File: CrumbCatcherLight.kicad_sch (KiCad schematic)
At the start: 10 parts, among them J1 USB_C_Receptacle, U0 PCB, U1 ECMF02-2AMX6

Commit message: Clear ERC's
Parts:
- renumbered U0 to U2
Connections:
- no-connect marks 16 -> 17
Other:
- sheet RP2040: file mad_lib/schematics/MCU/MCU_RP2040.kicad_sch -> mad_lib/schematics/Keyboard Controllers/Controller_RP2040.kicad_sch
- sheet RP2040 ports: added LED_DO; removed none
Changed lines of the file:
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@@
 	)
 	(no_connect
+		(at 177.165 104.14)
+	)
+	(no_connect
 		(at 175.26 69.85)
 	)
@@
 	(wire
 		(pts
+			(xy 172.72 104.14) (xy 177.165 104.14)
+		)
+		(stroke
+			(width 0)
+			(type default)
+		)
+	)
+	(wire
+		(pts
 			(xy 47.625 57.785) (xy 48.895 57.785)
 		)
@@
 		(dnp no)
 		(fields_autoplaced yes)
-		(property "Reference" "#PWR07"
+		(property "Reference" "#PWR05"
 			(at 149.86 62.23 0)
 			(effects
@@
 			(project "CrumbCatcherLight"
 				(path "/eedae293-eb5b-47bd-b383-bccfdf81bf72"
-					(reference "#PWR07")
+					(reference "#PWR05")
 					(unit 1)
 				)
@@
 		(on_board yes)
 		(dnp no)
-		(property "Reference" "U0"
+		(property "Reference" "U2"
 			(at 171.45 190.4999 0)
 			(effects
@@
 			(project "CrumbCatcherLight"
 				(path "/eedae293-eb5b-47bd-b383-bccfdf81bf72"
-					(reference "U0")
+					(reference "U2")
 					(unit 1)
 				)
@@
 		(dnp no)
 		(fields_autoplaced yes)
-		(property "Reference" "#PWR08"
+		(property "Reference" "#PWR07"
 			(at 184.785 61.595 0)
 			(effects
@@
 			(project "CrumbCatcherLight"
 				(path "/eedae293-eb5b-47bd-b383-bccfdf81bf72"
-					(reference "#PWR08")
+					(reference "#PWR07")
 					(unit 1)
 				)
@@
 		(on_board yes)
 		(dnp no)
-		(property "Reference" "#PWR09"
+		(property "Reference" "#PWR06"
 			(at 150.495 114.935 0)
 			(effects
@@
 			(project "CrumbCatcherLight"
 				(path "/eedae293-eb5b-47bd-b383-bccfdf81bf72"
-					(reference "#PWR09")
+					(reference "#PWR06")
 					(unit 1)
 				)
@@
 		(on_board yes)
 		(dnp no)
-		(property "Reference" "#PWR05"
+		(property "Reference" "#PWR08"
 			(at 185.42 114.935 0)
 			(effects
@@
 			(project "CrumbCatcherLight"
 				(path "/eedae293-eb5b-47bd-b383-bccfdf81bf72"
-					(reference "#PWR05")
+					(reference "#PWR08")
 					(unit 1)
 				)
@@
 			)
 		)
-		(property "Sheetfile" "mad_lib/schematics/MCU/MCU_RP2040.kicad_sch"
+		(property "Sheetfile" "mad_lib/schematics/Keyboard Controllers/Controller_RP2040.kicad_sch"
 			(at 153.67 107.8996 0)
 			(effects
@@
 			)
 		)
+		(pin "LED_DO" output
+			(at 172.72 104.14 0)
+			(effects
+				(font
+					(size 1.27 1.27)
+				)
+				(justify right)
+			)
+		)
 		(instances
 			(project "CrumbCatcherLight"
 				(path "/eedae293-eb5b-47bd-b383-bccfdf81bf72"
-					(page "2")
+					(page "4")
 				)
 			)

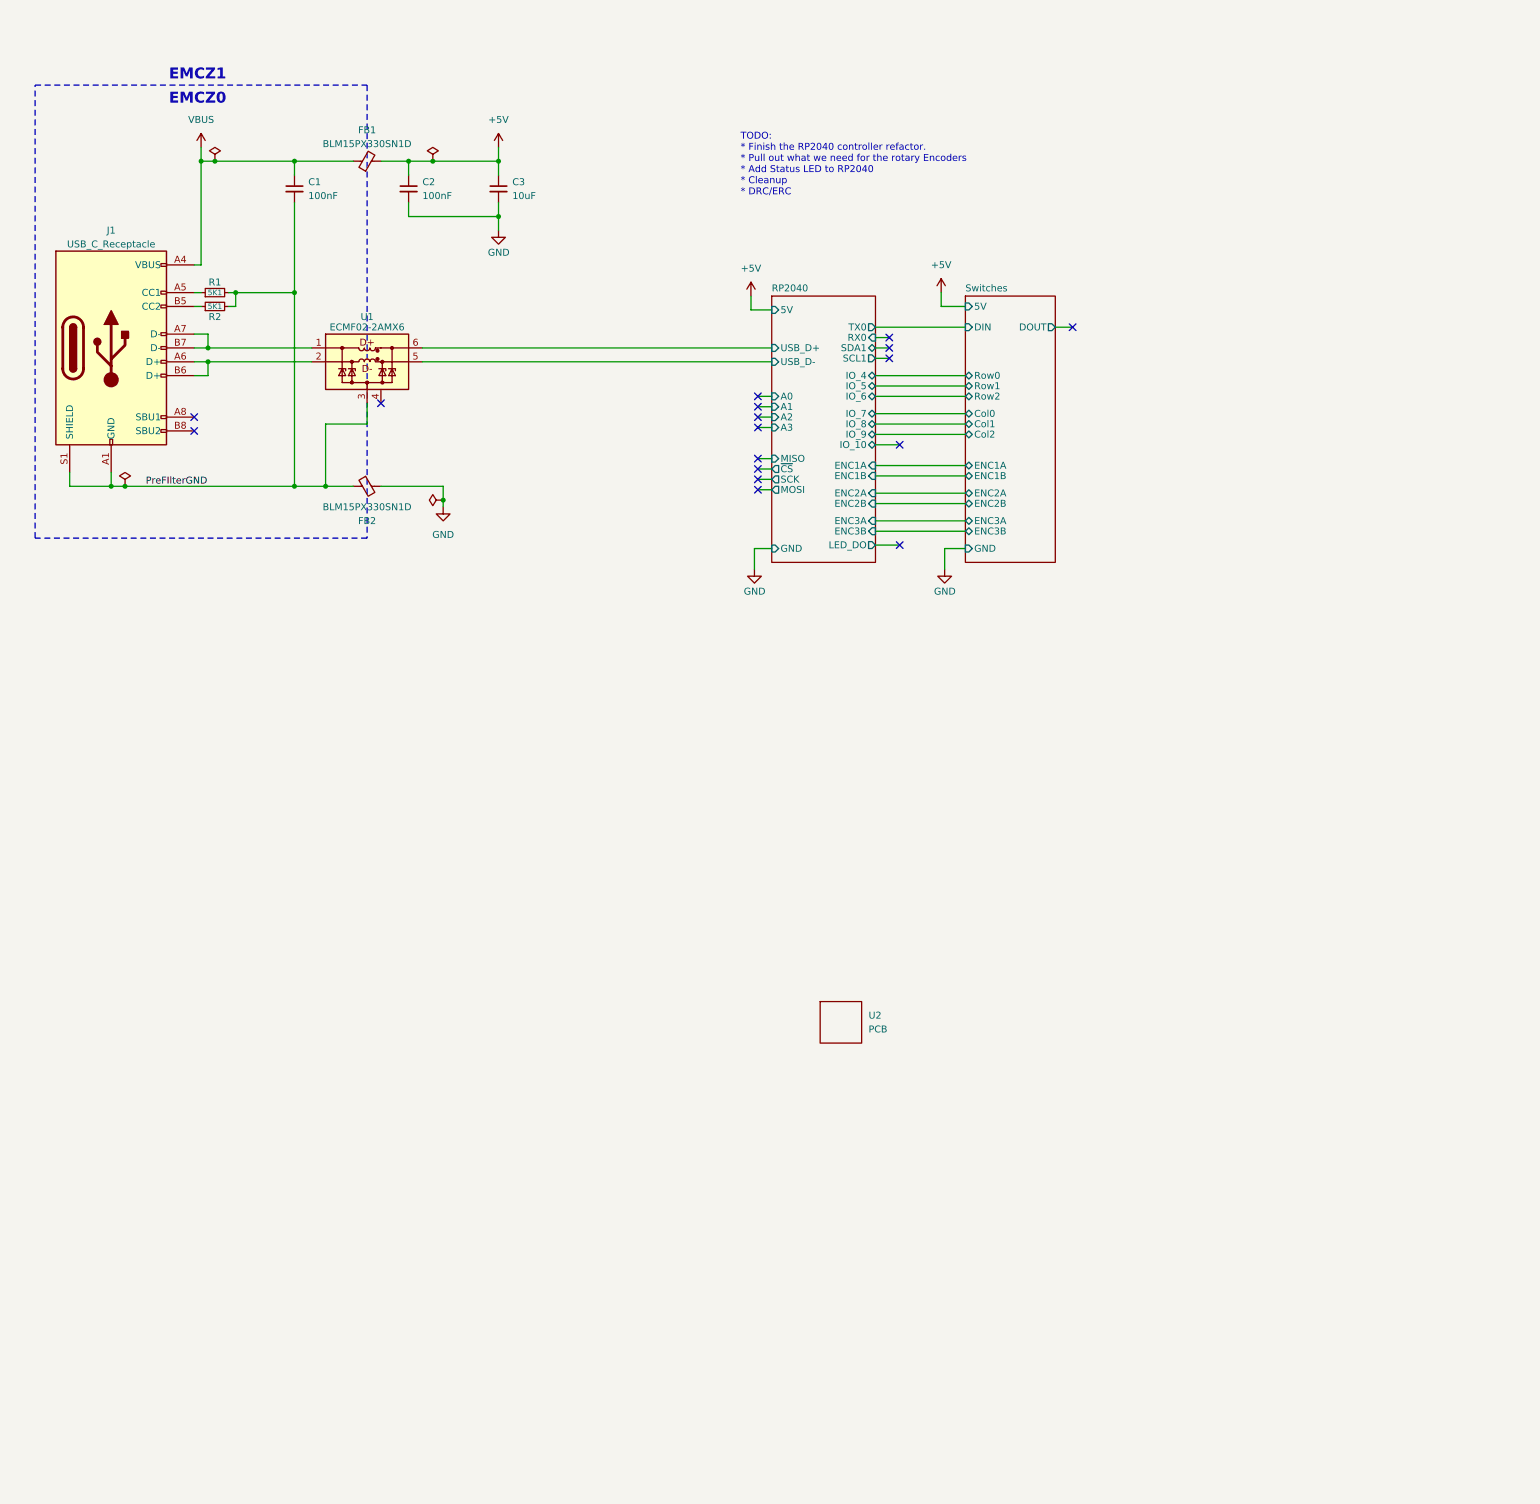
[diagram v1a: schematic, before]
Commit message: Add some reference circuits, add bq240xx, start to addnRF52840
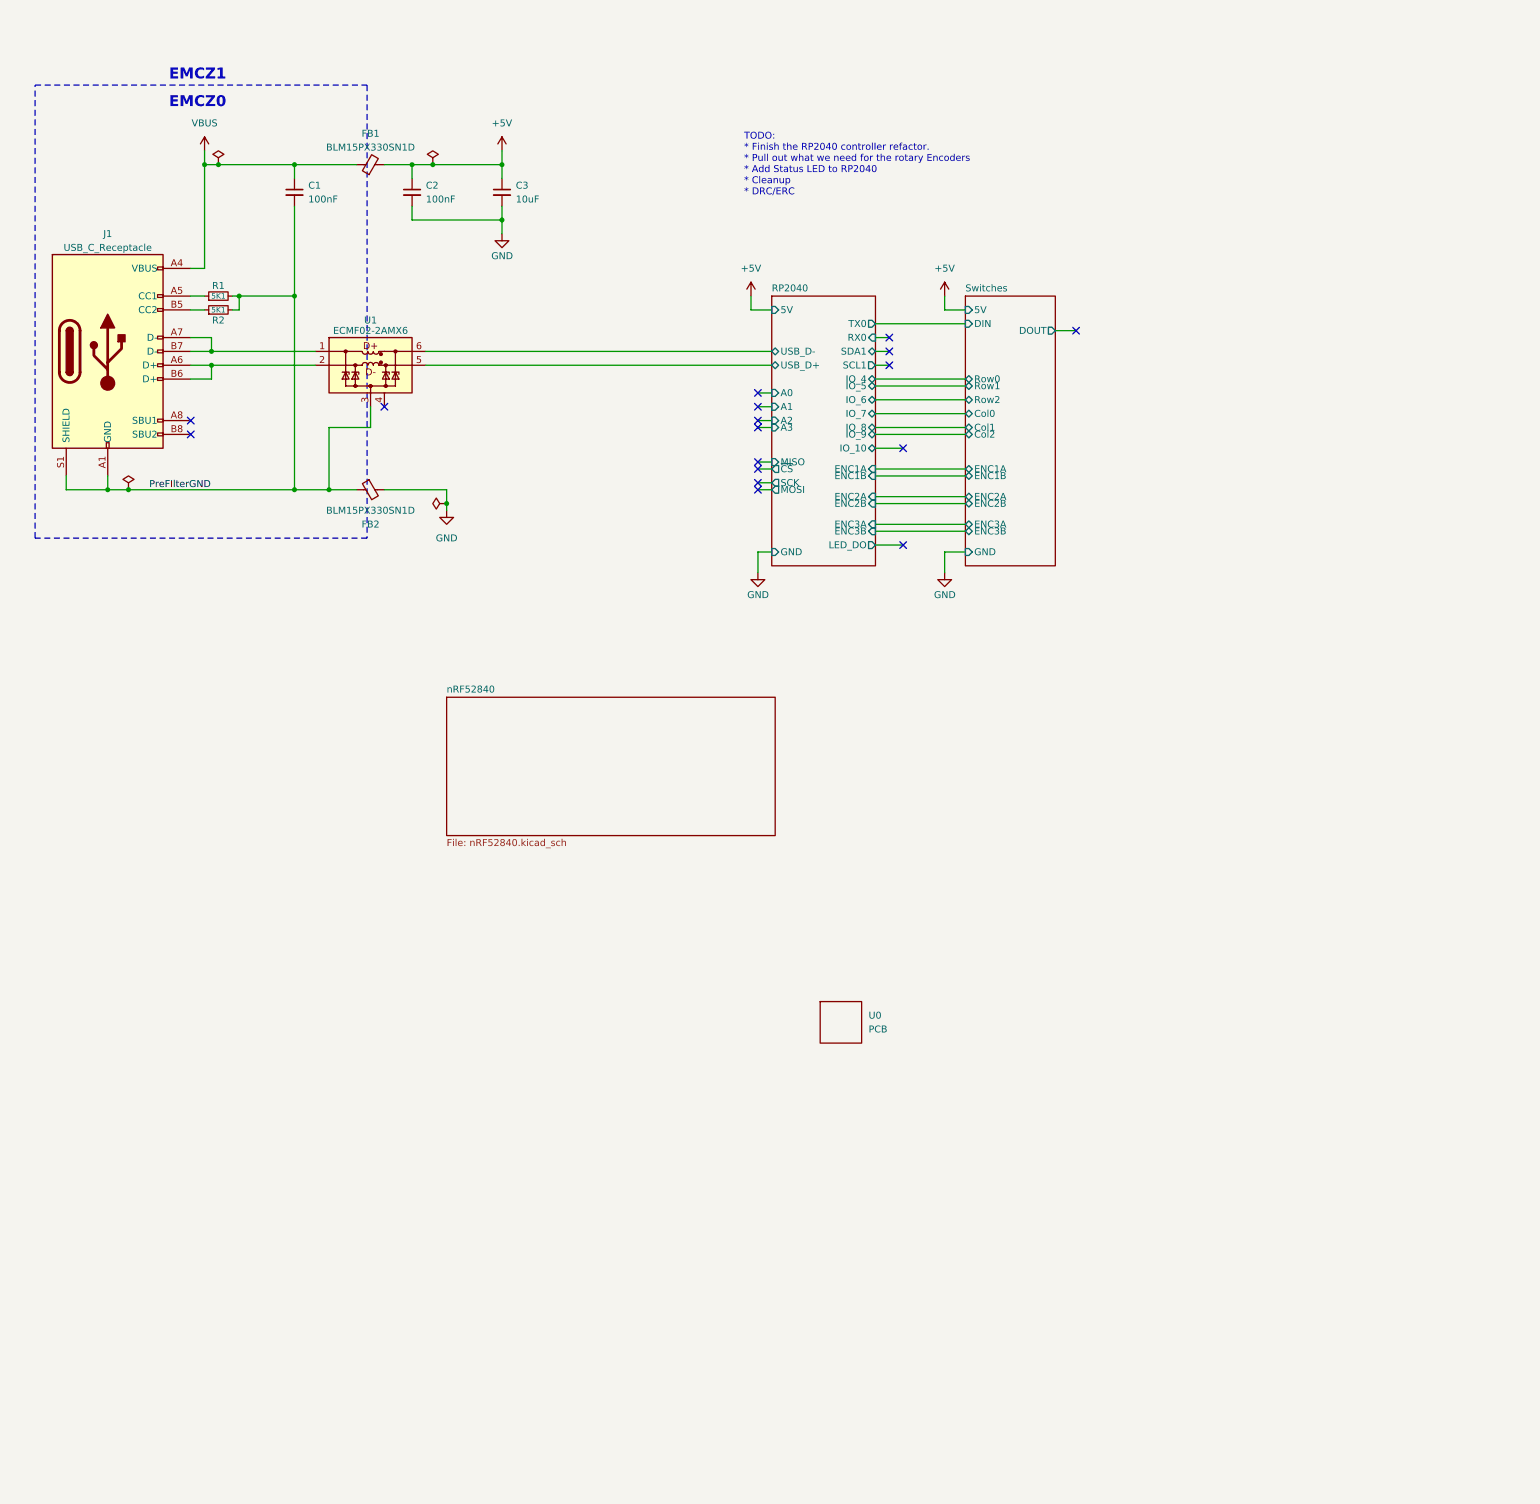
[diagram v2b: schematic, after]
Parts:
- renumbered U2 to U0
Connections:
- net RP2040/USB_D+: now also U1.5 (D-_out); no longer U1.6 (D+_out)
- net RP2040/USB_D-: now also U1.6 (D+_out); no longer U1.5 (D-_out)
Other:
- added sheet nRF52840 (nRF52840.kicad_sch)
- moved on the sheet: C1, C2, C3, FB1, FB2, J1, R1, R2, U1

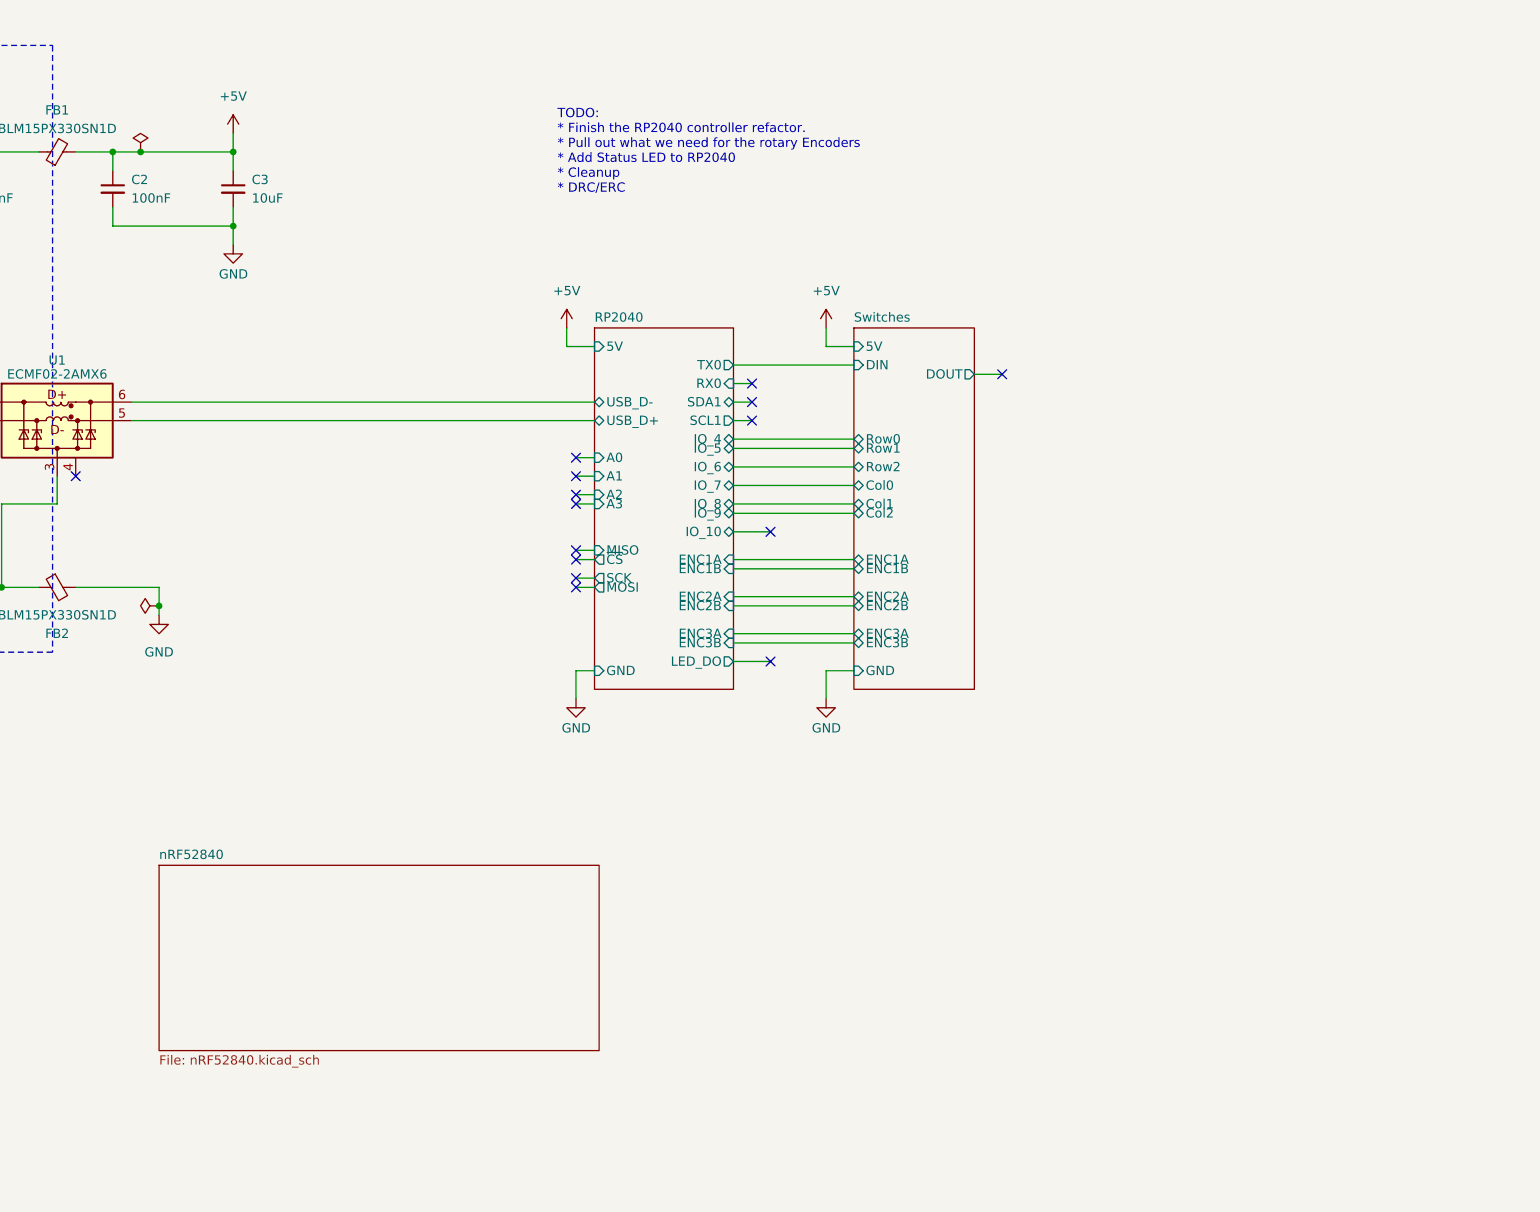
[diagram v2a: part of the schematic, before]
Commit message: Update to nRF52840 module, add BQ for battery charging
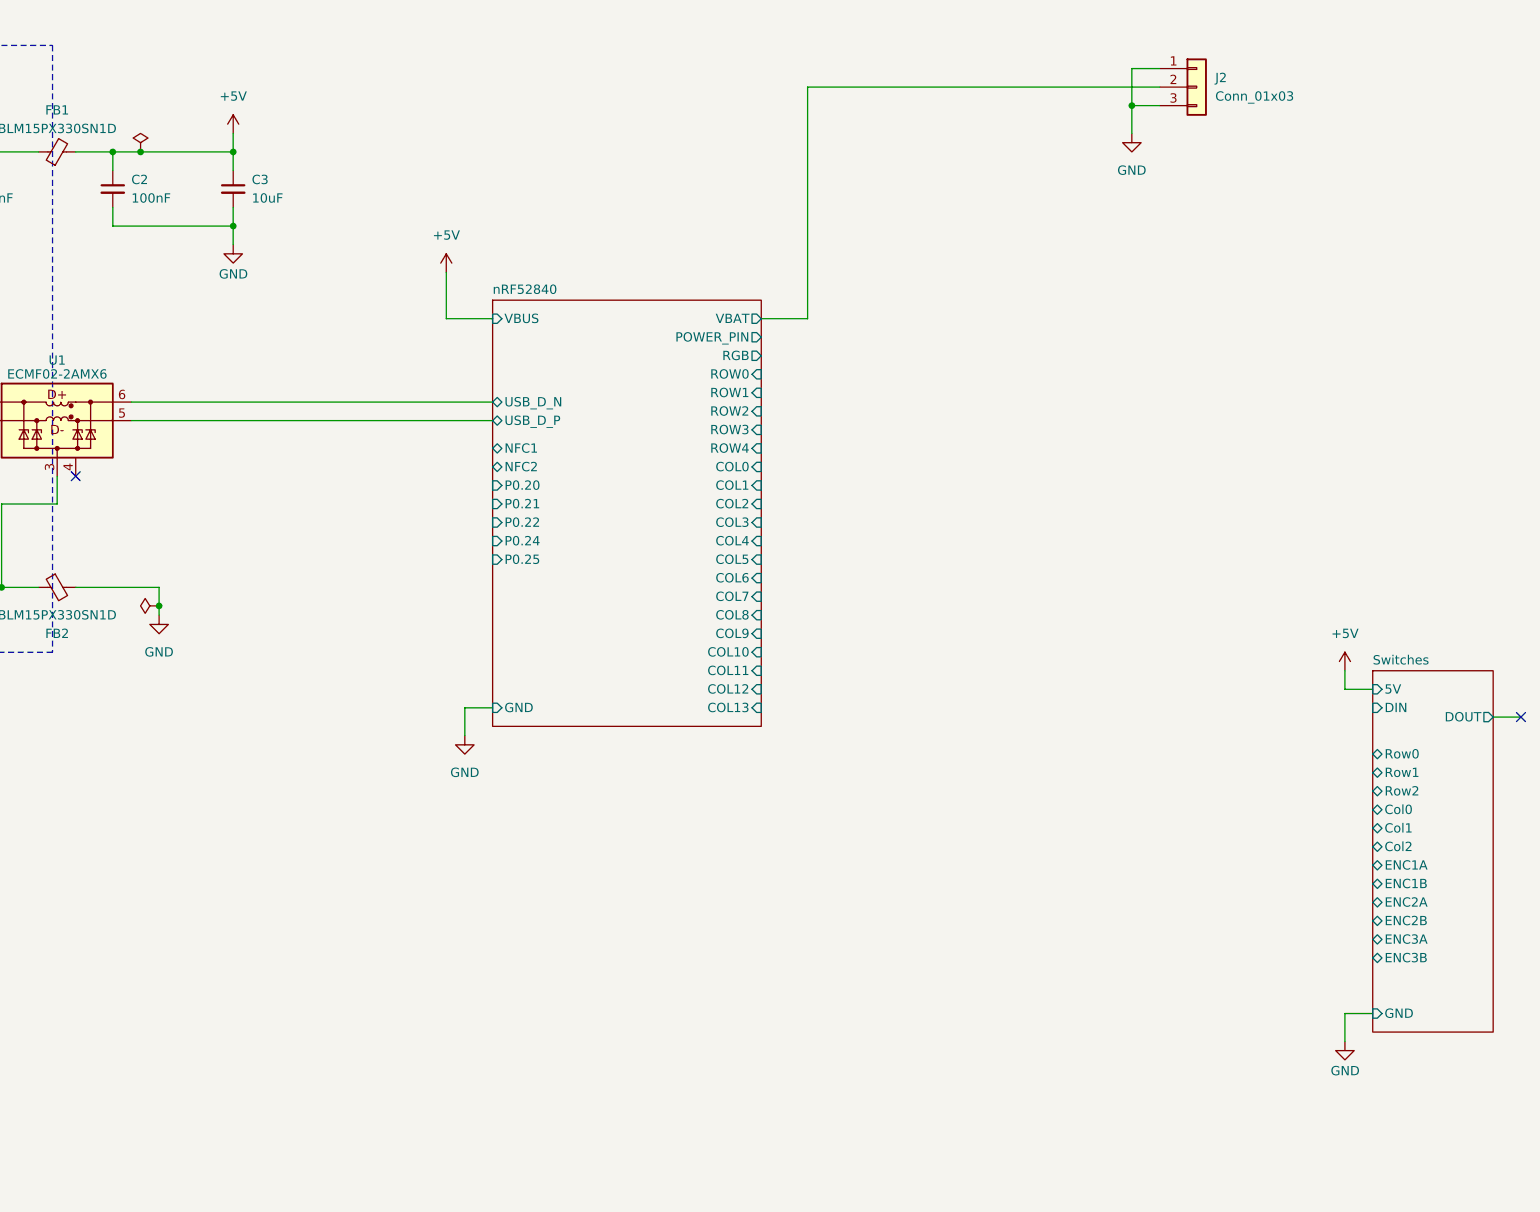
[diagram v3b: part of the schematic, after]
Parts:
- added J2: Conn_01x03, Connector_JST:JST_PH_B3B-PH-SM4-TB_1x03-1MP_P2.00mm_Vertical, symbol Connector_Generic:Conn_01x03
- C3: LCSC (none) -> C2932476; digikey (none) -> 311-1869-1-ND; mouser (none) -> 603-CC805KKX5R8BB106
- J1: Price $1.29 -> $1.29
- R1, R2: Price $0.16 -> $0.16
- U1: Price $0.83 -> $0.83
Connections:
- net GND: now also J2.1 (Pin_1), J2.3 (Pin_3)
- net RP2040/USB_D+ renamed nRF52840/USB_D_P
- net RP2040/USB_D- renamed nRF52840/USB_D_N
- new net nRF52840/VBAT: J2.2 (Pin_2)
- no-connect marks 17 -> 4
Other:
- removed sheet RP2040
- sheet nRF52840 ports: added COL0, COL1, COL10, COL11, COL12, COL13, COL2, COL3, COL4, COL5, COL6, COL7, COL8, COL9, GND, NFC1, NFC2, P0.20, P0.21, P0.22, P0.24, P0.25, POWER_PIN, RGB, ROW0, ROW1, ROW2, ROW3, ROW4, USB_D_N, USB_D_P, VBAT, VBUS; removed none
- note removed: "TODO: * Finish the RP2040 controller refactor. * Pull out what we need for the rotary Encoders * Add Status LED to RP2040 * Cleanup * DRC/ERC"

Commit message: More research, added connector for Qi charger in
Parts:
- added D1, D2: MBR1020VL, Diode_SMD:D_SOD-123F, symbol Diode:MBR1020VL
- added J4: Qi Charger In, Connector_JST:JST_PH_B3B-PH-SM4-TB_1x03-1MP_P2.00mm_Vertical, symbol Connector_Generic:Conn_01x02
- added R21: 10K, Resistor_SMD:R_0603_1608Metric, symbol Device:R_Small
- J2: value Conn_01x03 -> Mating Half to 51021-0300
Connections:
- net +5V: now also D1.1 (K), D2.1 (K); no longer FB1.2
- net GND: now also J4.2 (Pin_2), R21.2; no longer J2.1 (Pin_1)
- net nRF52840/VBAT renamed Battery Charger/BATT_TS
- net Battery Charger/BATT_TS: now also R21.1
- new net: D2.2 (A), J4.1 (Pin_1)
- new net: D1.2 (A), FB1.2
- new net Battery Charger/VBAT: J2.1 (Pin_1)
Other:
- added sheet Battery Charger (BQ24075.kicad_sch)
- sheet nRF52840 ports: added none; removed VBAT, VBUS
- note added: "51021-0300"
- note added: "Check if the 1020 is equivalent replacement"
- note added: "LP286380"
- note added: "MBR120"
- moved on the sheet: C2, C3, J2
